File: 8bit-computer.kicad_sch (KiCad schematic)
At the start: 10 parts

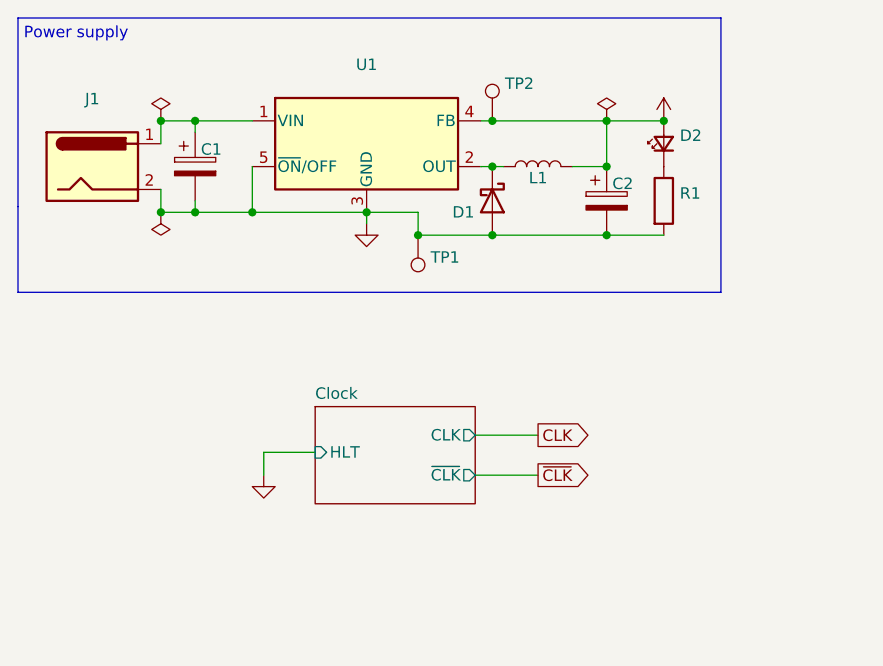
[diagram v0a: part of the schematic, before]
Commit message: 🚧 replace power supply with USB-C socket
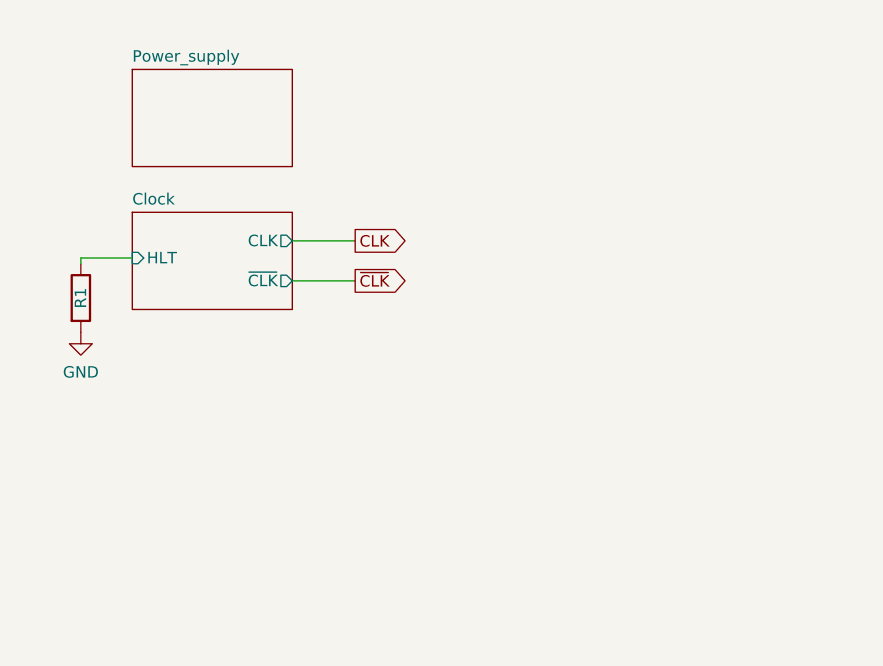
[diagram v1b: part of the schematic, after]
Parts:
- removed C1, C2: (no value), symbol Device:C_Polarized
- removed D1: (no value), symbol Diode:1N5822
- removed D2: (no value), symbol Device:LED_Small
- removed J1: (no value), symbol Connector:Jack-DC
- removed L1: (no value), symbol Device:L
- removed TP1, TP2: (no value), symbol Connector:TestPoint
- removed U1: (no value), symbol Regulator_Switching:LM2576T-5
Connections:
- net Clock/HLT: now reaches R1.1
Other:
- added sheet Power_supply (power_supply.kicad_sch)
- note removed: "Power supply"
